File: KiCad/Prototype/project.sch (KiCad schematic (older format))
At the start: 72 parts, among them J1 Barrel_Jack, J10 POT 2, J11 POT 3, J12 POT 4, J13 POT 5, J14 PRESSURE, J15 MIDI IN, J16 MIDI OUT, J17 POT 6, J18 POT 7, J19 POT 8, J2 USB_B, J3 ICSP, J4 BANK 0..7, J5 BANK 8..15, J6 EXPRESSION, J7 SUSTAIN, J8 PD6/ADC9/SPEAKER, J9 POT 1, Q1 PMOS, SW1 RESET, U1 LP2985-3.3, U10 HCPL-0600, U2 LMV358, U3 NCP1117-1.5, U4 ATMEGA32U4-AU, U5 74LS138, U6 74LS138, U7 74LS238, U8 74LS238, U9 74HC04, Y1 16 Mhz

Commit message: more routing
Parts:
- RN1, RN2: footprint footprints:R_Cat16-8 -> footprints:SOIC-16_4.55x10.3mm_P1.27mm
- U5, U6, U7, U8: footprint footprints:TSSOP-16_4.4x5mm_P0.65mm -> footprints:SOIC-16_4.55x10.3mm_P1.27mm
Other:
- moved on the sheet: RN1
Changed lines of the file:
@@
 F 0 "U6" H 2300 10200 50  0000 C CNN
 F 1 "74LS138" H 2300 10100 50  0000 C CNN
-F 2 "footprints:TSSOP-16_4.4x5mm_P0.65mm" H 2100 9650 50  0001 C CNN
+F 2 "footprints:SOIC-16_4.55x10.3mm_P1.27mm" H 2100 9650 50  0001 C CNN
 F 3 "http://www.ti.com/lit/gpn/sn74LS138" H 2100 9650 50  0001 C CNN
 	1    2100 9650
@@
 F 0 "U5" H 2300 8350 50  0000 C CNN
 F 1 "74LS138" H 2300 8250 50  0000 C CNN
-F 2 "footprints:TSSOP-16_4.4x5mm_P0.65mm" H 2100 7800 50  0001 C CNN
+F 2 "footprints:SOIC-16_4.55x10.3mm_P1.27mm" H 2100 7800 50  0001 C CNN
 F 3 "http://www.ti.com/lit/gpn/sn74LS138" H 2100 7800 50  0001 C CNN
 	1    2100 7800
@@
 F 0 "U8" H 5750 10200 50  0000 C CNN
 F 1 "74LS238" H 5750 10100 50  0000 C CNN
-F 2 "footprints:TSSOP-16_4.4x5mm_P0.65mm" H 5550 9650 50  0001 C CNN
+F 2 "footprints:SOIC-16_4.55x10.3mm_P1.27mm" H 5550 9650 50  0001 C CNN
 F 3 "http://www.ti.com/lit/gpn/sn74LS138" H 5550 9650 50  0001 C CNN
 	1    5550 9650
@@
 F 0 "U7" H 5750 8350 50  0000 C CNN
 F 1 "74LS238" H 5750 8250 50  0000 C CNN
-F 2 "footprints:TSSOP-16_4.4x5mm_P0.65mm" H 5550 7800 50  0001 C CNN
+F 2 "footprints:SOIC-16_4.55x10.3mm_P1.27mm" H 5550 7800 50  0001 C CNN
 F 3 "http://www.ti.com/lit/gpn/sn74LS138" H 5550 7800 50  0001 C CNN
 	1    5550 7800
@@
 F 0 "RN2" H 15450 7250 50  0000 L CNN
 F 1 "10k/4k7" H 15450 7150 50  0000 L CNN
-F 2 "footprints:R_Cat16-8" V 15425 7200 50  0001 C CNN
+F 2 "footprints:SOIC-16_4.55x10.3mm_P1.27mm" V 15425 7200 50  0001 C CNN
 F 3 "http://www.farnell.com/datasheets/1885635.pdf?_ga=2.1905073.1038136674.1585932994-1945507881.1583328620" H 15050 7200 50  0001 C CNN
 	1    15050 7200
@@
 MIDI in/out
 Wire Wire Line
-	7750 6050 7400 6050
-Wire Wire Line
-	7750 6150 7400 6150
-Wire Wire Line
-	7750 6250 7400 6250
-Wire Wire Line
-	7750 6350 7400 6350
-Wire Wire Line
-	7750 6450 7400 6450
-Wire Wire Line
-	7750 6550 7400 6550
-Wire Wire Line
-	7750 6650 7400 6650
-Wire Wire Line
-	7750 6750 7400 6750
-Wire Wire Line
-	8150 6050 8250 6050
-Text Label 7400 6050 0    60   ~ 0
+	3900 5950 3550 5950
+Wire Wire Line
+	3900 6050 3550 6050
+Wire Wire Line
+	3900 6150 3550 6150
+Wire Wire Line
+	3900 6250 3550 6250
+Wire Wire Line
+	3900 6350 3550 6350
+Wire Wire Line
+	3900 6450 3550 6450
+Wire Wire Line
+	3900 6550 3550 6550
+Wire Wire Line
+	3900 6650 3550 6650
+Wire Wire Line
+	4300 5950 4400 5950
+Text Label 3550 5950 0    60   ~ 0
 PB0
-Text Label 7400 6150 0    60   ~ 0
+Text Label 3550 6050 0    60   ~ 0
 PB1
-Text Label 7400 6250 0    60   ~ 0
+Text Label 3550 6150 0    60   ~ 0
 PB2
-Text Label 7400 6350 0    60   ~ 0
+Text Label 3550 6250 0    60   ~ 0
 PB3
-Text Label 7400 6450 0    60   ~ 0
+Text Label 3550 6350 0    60   ~ 0
 PB4
-Text Label 7400 6550 0    60   ~ 0
+Text Label 3550 6450 0    60   ~ 0
 PB5
-Text Label 7400 6650 0    60   ~ 0
+Text Label 3550 6550 0    60   ~ 0
 PB6
-Text Label 7400 6750 0    60   ~ 0
+Text Label 3550 6650 0    60   ~ 0
 PB7
 $Comp
@@
 Text Label 10650 4200 0    60   ~ 0
 ADC9
-Text Notes 7400 5600 0    60   ~ 0
+Text Notes 3550 5500 0    60   ~ 0
 Keyboard scanning pullups
 Text Notes 10600 3950 0    60   ~ 0
@@
 L Device:R_Pack08 RN1
 U 1 1 5EF332C4
-P 7950 6450
-F 0 "RN1" V 7300 6400 50  0000 L CNN
-F 1 "4k7" V 7400 6400 50  0000 L CNN
-F 2 "footprints:R_Cat16-8" V 8325 6450 50  0001 C CNN
-F 3 "http://www.farnell.com/datasheets/1885635.pdf?_ga=2.1905073.1038136674.1585932994-1945507881.1583328620" H 7950 6450 50  0001 C CNN
-	1    7950 6450
-	0    1    1    0
+P 4100 6350
+F 0 "RN1" V 3450 6300 50  0000 L CNN
+F 1 "4k7" V 3550 6300 50  0000 L CNN
+F 2 "footprints:SOIC-16_4.55x10.3mm_P1.27mm" V 4475 6350 50  0001 C CNN
+F 3 "http://www.farnell.com/datasheets/1885635.pdf?_ga=2.1905073.1038136674.1585932994-1945507881.1583328620" H 4100 6350 50  0001 C CNN
+	1    4100 6350
+	0    -1   1    0
 $EndComp
 NoConn ~ 15250 7000
@@
 L project:+5V #PWR053
 U 1 1 5EA3FF16
-P 8300 6050
-F 0 "#PWR053" H 8300 5900 50  0001 C CNN
-F 1 "+5V" H 8300 6190 50  0000 C CNN
-F 2 "" H 8300 6050 50  0001 C CNN
-F 3 "" H 8300 6050 50  0001 C CNN
-	1    8300 6050
+P 4450 5950
+F 0 "#PWR053" H 4450 5800 50  0001 C CNN
+F 1 "+5V" H 4450 6090 50  0000 C CNN
+F 2 "" H 4450 5950 50  0001 C CNN
+F 3 "" H 4450 5950 50  0001 C CNN
+	1    4450 5950
 	0    1    1    0
 $EndComp
 Wire Wire Line
-	8150 6150 8250 6150
-Wire Wire Line
-	8250 6150 8250 6050
-Connection ~ 8250 6050
-Wire Wire Line
-	8250 6050 8300 6050
-Wire Wire Line
-	8150 6250 8250 6250
-Wire Wire Line
-	8250 6250 8250 6150
-Connection ~ 8250 6150
-Wire Wire Line
-	8150 6350 8250 6350
-Wire Wire Line
-	8250 6350 8250 6250
-Connection ~ 8250 6250
-Wire Wire Line
-	8150 6450 8250 6450
-Wire Wire Line
-	8250 6450 8250 6350
-Connection ~ 8250 6350
-Wire Wire Line
-	8150 6550 8250 6550
-Wire Wire Line
-	8250 6550 8250 6450
-Connection ~ 8250 6450
-Wire Wire Line
-	8150 6650 8250 6650
-Wire Wire Line
-	8250 6650 8250 6550
-Connection ~ 8250 6550
-Wire Wire Line
-	8150 6750 8250 6750
-Wire Wire Line
-	8250 6750 8250 6650
-Connection ~ 8250 6650
+	4300 6050 4400 6050
+Wire Wire Line
+	4400 6050 4400 5950
+Connection ~ 4400 5950
+Wire Wire Line
+	4400 5950 4450 5950
+Wire Wire Line
+	4300 6150 4400 6150
+Wire Wire Line
+	4400 6150 4400 6050
+Connection ~ 4400 6050
+Wire Wire Line
+	4300 6250 4400 6250
+Wire Wire Line
+	4400 6250 4400 6150
+Connection ~ 4400 6150
+Wire Wire Line
+	4300 6350 4400 6350
+Wire Wire Line
+	4400 6350 4400 6250
+Connection ~ 4400 6250
+Wire Wire Line
+	4300 6450 4400 6450
+Wire Wire Line
+	4400 6450 4400 6350
+Connection ~ 4400 6350
+Wire Wire Line
+	4300 6550 4400 6550
+Wire Wire Line
+	4400 6550 4400 6450
+Connection ~ 4400 6450
+Wire Wire Line
+	4300 6650 4400 6650
+Wire Wire Line
+	4400 6650 4400 6550
+Connection ~ 4400 6550
 NoConn ~ 11650 6000
 NoConn ~ 11500 6800

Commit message: committing older misc changes
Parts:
- J2: symbol Connector:USB_B -> project-rescue:USB_B-Connector
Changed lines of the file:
@@
 +5V
 $Comp
-L Connector:USB_B J2
+L project-rescue:USB_B-Connector J2
 U 1 1 5E95986C
 P 4600 2650

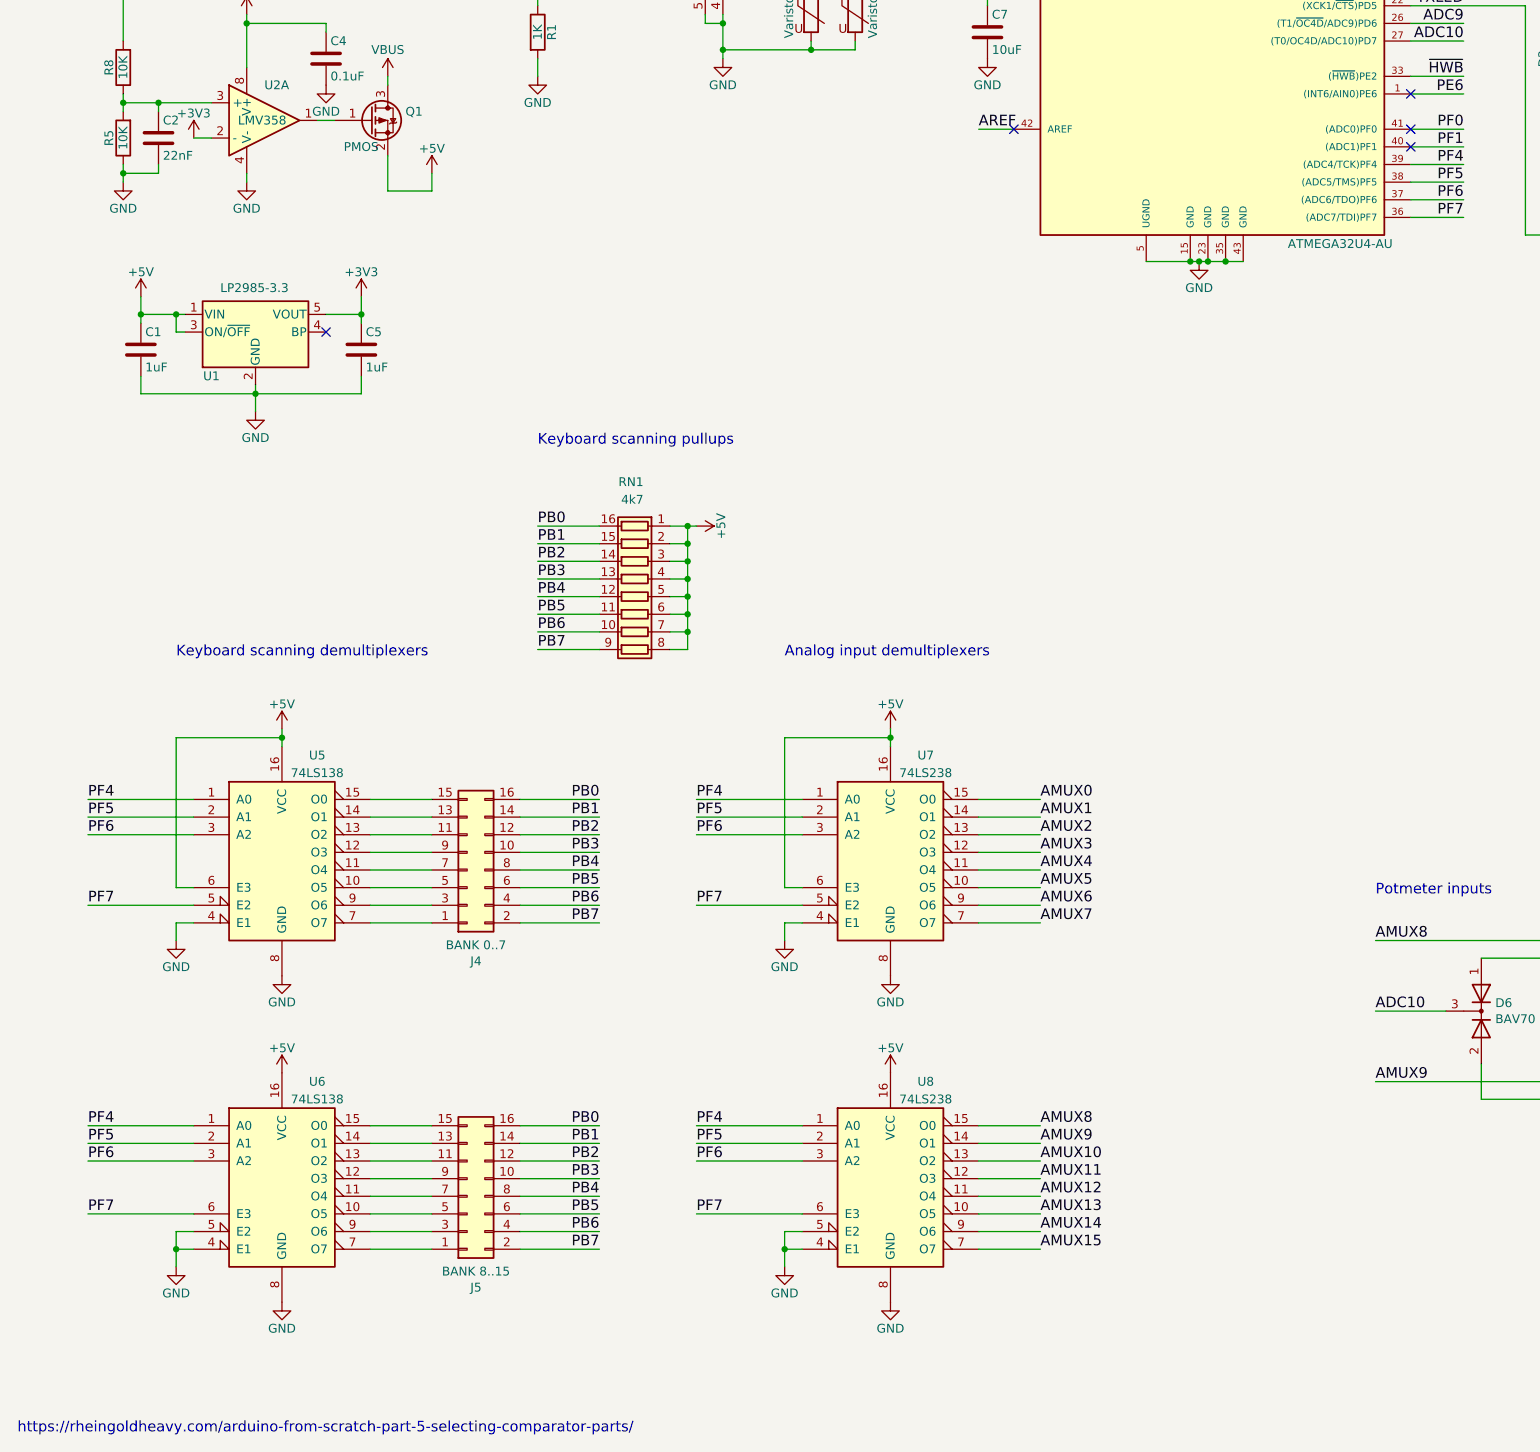
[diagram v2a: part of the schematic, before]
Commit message: Removed unneccessary 3V3 regulator Added latch for ADC multiplexing
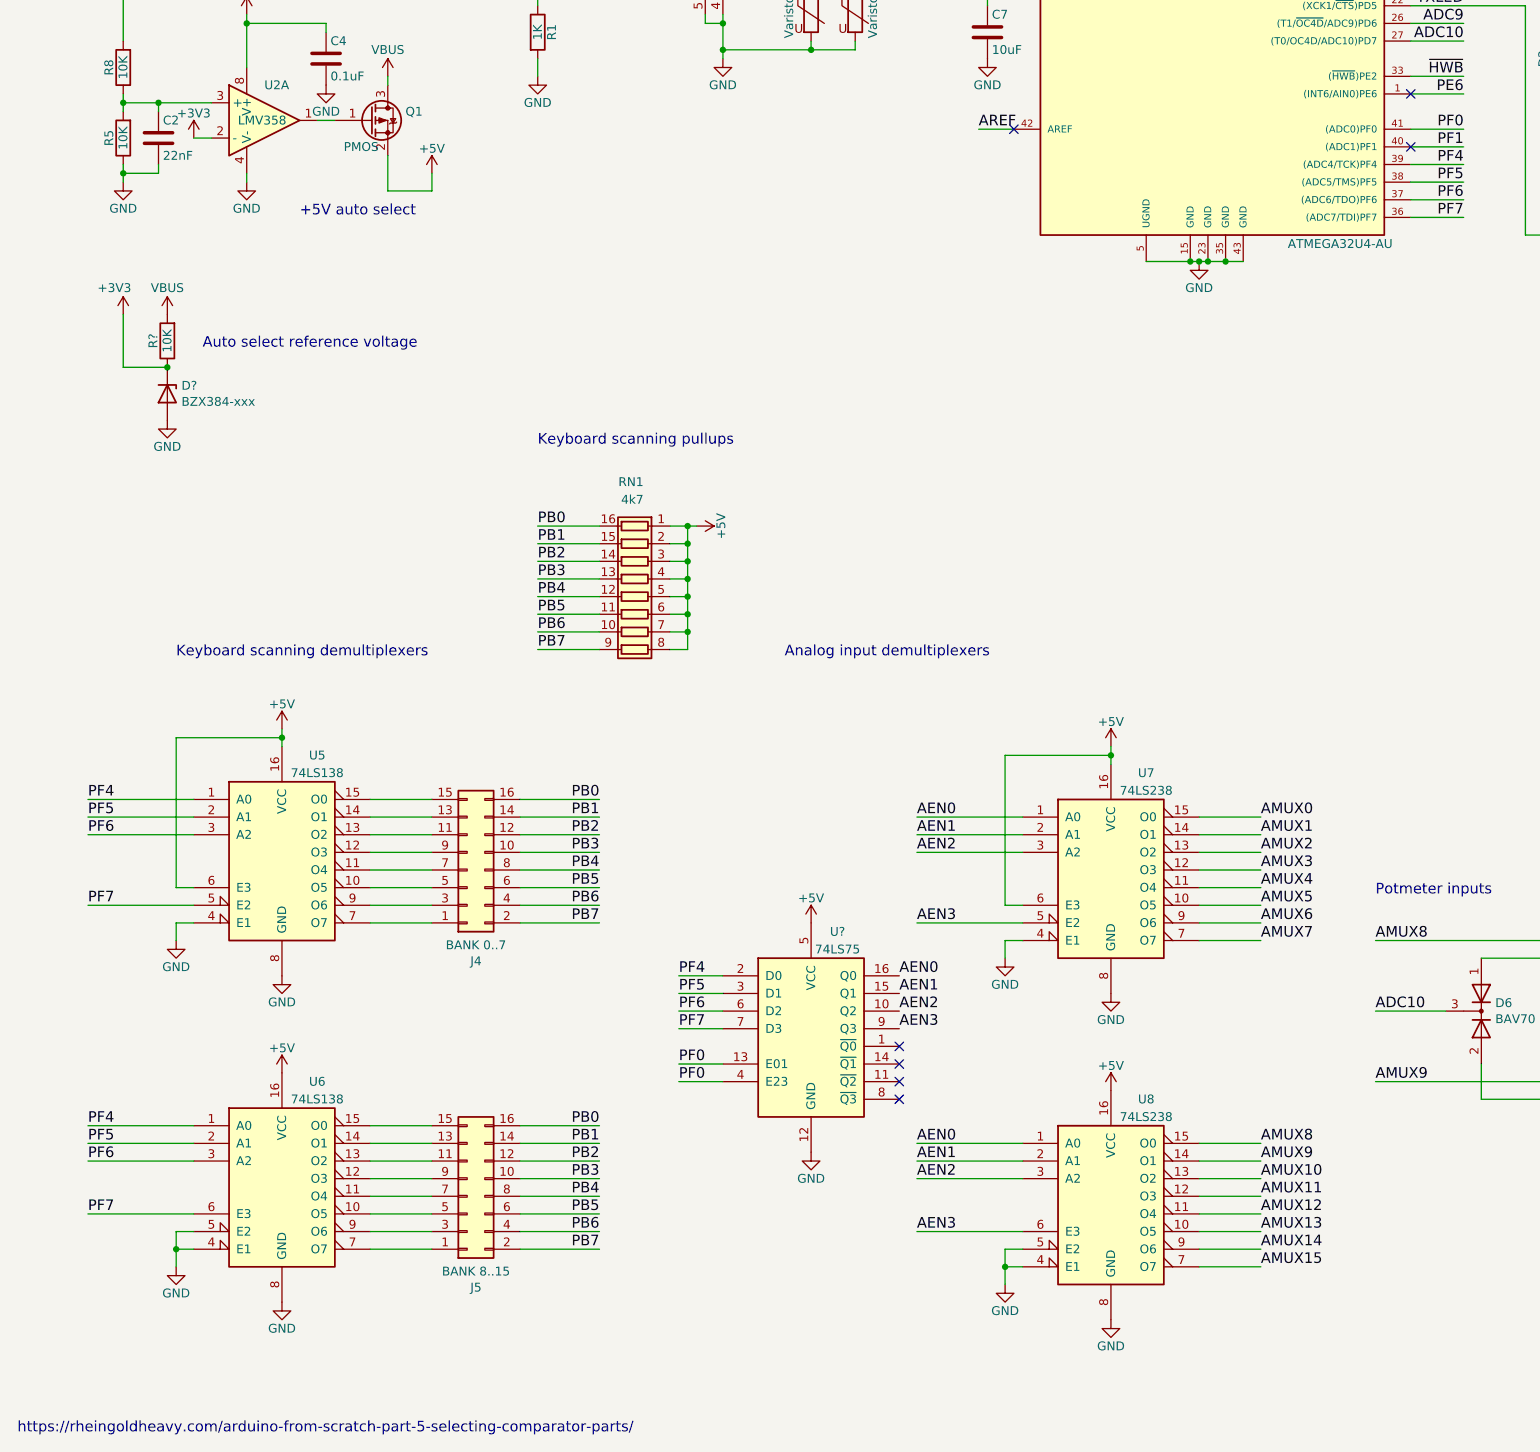
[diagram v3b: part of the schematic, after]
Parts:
- removed C1, C5: 1uF, footprints:C_0805_HandSoldering, symbol project:C
- removed U1: LP2985-3.3, footprints:SOT-23-5, symbol project:LP2985-3.3
- added D?: BZX384-xxx, Diode_SMD:D_SOD-323, symbol Diode:BZX384-xxx
- added R?: 10K, footprints:R_0805_HandSoldering, symbol project:R
- added U?: 74LS75, symbol 74xx:74LS75
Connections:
- net +3V3: now also D?.1 (K), R?.1
- net +5V: now also U?.5 (VCC)
- net GND: now also D?.2 (A), U?.12 (GND)
- net PF0: now also U?.13 (E01), U?.4 (E23)
- net PF4: now also U?.2 (D0); no longer U7.1 (A0), U8.1 (A0)
- net PF5: now also U?.3 (D1); no longer U7.2 (A1), U8.2 (A1)
- net PF6: now also U?.6 (D2); no longer U7.3 (A2), U8.3 (A2)
- net PF7: now also U?.7 (D3); no longer U7.5 (E2), U8.6 (E3)
- net VBUS: now also R?.2
- new net AEN0: U7.1 (A0), U8.1 (A0), U?.16 (Q0)
- new net AEN1: U7.2 (A1), U8.2 (A1), U?.15 (Q1)
- new net AEN2: U7.3 (A2), U8.3 (A2), U?.10 (Q2)
- new net AEN3: U7.5 (E2), U8.6 (E3), U?.9 (Q3)
- no-connect marks 23 -> 25
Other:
- note added: "+5V auto select"
- note added: "Auto select reference voltage"
- moved on the sheet: U7, U8

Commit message: Readying schematic and routing for prototype production
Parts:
- U1: renamed from U?; footprint (none) -> footprints:SOIC-16_4.55x10.3mm_P1.27mm
- gave numbers to parts that had none: 2
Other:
- note added: "Analog input multiplexing"
- note added: "Internal/Pressure sensor inputs"
- note added: "Keyboard scanning multiplexing"
- note removed: "Analog input demultiplexers"
- note removed: "Keyboard scanning demultiplexers"
- note removed: "Keyboard scanning pullups"
- note removed: "Pressure sensor inputs"
- moved on the sheet: D10, D11, D13, D3, D5, D6, D7, D8, D9, J10, J11, J12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

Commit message: more work towards production
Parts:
- removed JP1: BOOT, footprints:SolderJumper-3_P1.3mm_Bridged12_Pad1.0x1.5mm, symbol Jumper:Jumper_3_Bridged12
- added J20: TTL MIDI, footprints:Molex_KK-254_AE-6410-03A_1x03_P2.54mm_Vertical, symbol Connector_Generic:Conn_01x03
- added JP1: BOOT, Jumper:SolderJumper-2_P1.3mm_Open_Pad1.0x1.5mm, symbol Jumper:Jumper_2_Open
- added JP2: PULLUP, footprints:SolderJumper-3_P1.3mm_Bridged12_Pad1.0x1.5mm, symbol Jumper:Jumper_3_Bridged12
- C2: LCSC (none) -> C1729
- C3, C6, C7: LCSC (none) -> C13585
- C4: LCSC (none) -> C49678
- D1, D2, D4: LCSC (none) -> C84256
- D10, D11, D13, D6, D7, D8, D9: LCSC (none) -> C68978
- D12, D3, D5: footprint footprints:D_SOD-523 -> footprints:D_SOD-323; LCSC (none) -> C2128
- D14: value BZX384-xxx -> ZMM3V3; footprint Diode_SMD:D_SOD-323 -> Diode_SMD:D_MiniMELF; LCSC (none) -> C8056
- F1: value Polyfuse -> 0; LCSC (none) -> C17888
- J1: MOUSER (none) -> 490-PJ-102A
- J10, J11, J12, J13, J17, J18, J19, J9: MOUSER (none) -> 571-6404543
- J15, J16: MOUSER (none) -> 806-KCDX-5S-N2
- J2: MOUSER (none) -> 490-UJ2-BH-1-TH
- J3: MOUSER (none) -> 517-30306-6002HB
- J4, J5: MOUSER (none) -> 517-30316-6002
- J6, J7: MOUSER (none) -> 523-ACJS-MHOP
- J8: MOUSER (none) -> 571-640454-2
- Q1: value PMOS -> PMV48XP,215; LCSC (none) -> C75560
- R1, R2, R4: LCSC (none) -> C17513
- R10: LCSC (none) -> C17673
- R11, R5, R8: LCSC (none) -> C17414
- R13, R14, R15, R3: LCSC (none) -> C17557
- R16: value 1K -> 10K; LCSC (none) -> C17414
- R6, R7: LCSC (none) -> C17561
- R9: LCSC (none) -> C17514
- RV1, RV2: value Varistor -> P6SMB6.8CA; footprint footprints:R_0805_HandSoldering -> Diode_SMD:D_SMB; LCSC (none) -> C78395
- U10: MOUSER (none) -> 512-HCPL0600
- U3: value NCP1117-1.5 -> AMS1117-5.0; LCSC (none) -> C6187
- U4: MOUSER (none) -> 556-ATMEGA32U4-AU
- U5, U6: value 74LS138 -> 74HC138; MOUSER (none) -> 771-74HC138D
- U7, U8: value 74LS238 -> 74HC238; MOUSER (none) -> 771-74HC238D
- U9: MOUSER (none) -> 595-SN74HC04ANSRE4
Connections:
- net +5V: now also JP1.2 (B), JP2.1 (A); no longer RN1.1 (R1.1), RN1.2 (R2.1), RN1.3 (R3.1), RN1.4 (R4.1), RN1.5 (R5.1), RN1.6 (R6.1), RN1.7 (R7.1), RN1.8 (R8.1)
- net GND: now also R16.1, J20.1 (Pin_1), JP2.3 (B); no longer R16.2
- net RXD: now also J20.3 (Pin_3)
- net TXD: now also J20.2 (Pin_2)
- net ~HWB: now also R16.2, JP1.1 (A)
- net +3V3: no longer names the net of D14.1 (K), R11.1, U2.2 (-)
- new net: JP2.2 (C), RN1.1 (R1.1), RN1.2 (R2.1), RN1.3 (R3.1), RN1.4 (R4.1), RN1.5 (R5.1), RN1.6 (R6.1), RN1.7 (R7.1), RN1.8 (R8.1)
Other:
- moved on the sheet: D14, J3, R11, R16
